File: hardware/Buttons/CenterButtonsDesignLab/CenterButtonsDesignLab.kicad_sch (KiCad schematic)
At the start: 6 parts, among them J1 Conn_01x01, J2 Conn_01x01, J3 Conn_01x03, SW1 SW_Push, SW2 SW_Push, SW3 SW_Push

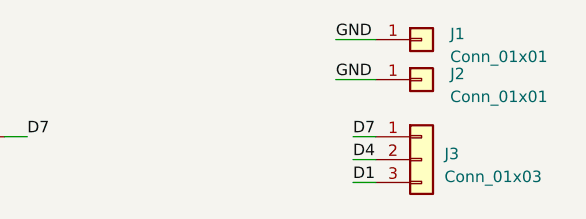
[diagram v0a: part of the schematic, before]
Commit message: BOM of buttons generated
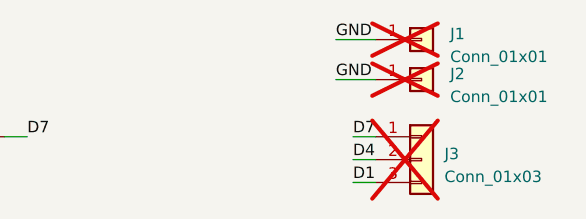
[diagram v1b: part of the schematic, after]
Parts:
- J1, J2, J3: now not fitted
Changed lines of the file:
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@@
   )
   (symbol (lib_id "Connector_Generic:Conn_01x01") (at 165.1 32.385 0) (unit 1)
-    (in_bom yes) (on_board yes) (dnp no) (fields_autoplaced)
+    (in_bom yes) (on_board yes) (dnp yes) (fields_autoplaced)
     (property "Reference" "J2" (at 168.275 31.75 0)
       (effects (font (size 1.27 1.27)) (justify left))
@@
   )
   (symbol (lib_id "Connector_Generic:Conn_01x03") (at 165.1 41.275 0) (unit 1)
-    (in_bom yes) (on_board yes) (dnp no) (fields_autoplaced)
+    (in_bom yes) (on_board yes) (dnp yes) (fields_autoplaced)
     (property "Reference" "J3" (at 167.64 40.64 0)
       (effects (font (size 1.27 1.27)) (justify left))
@@
   )
   (symbol (lib_id "Connector_Generic:Conn_01x01") (at 165.1 27.94 0) (unit 1)
-    (in_bom yes) (on_board yes) (dnp no) (fields_autoplaced)
+    (in_bom yes) (on_board yes) (dnp yes) (fields_autoplaced)
     (property "Reference" "J1" (at 168.275 27.305 0)
       (effects (font (size 1.27 1.27)) (justify left))

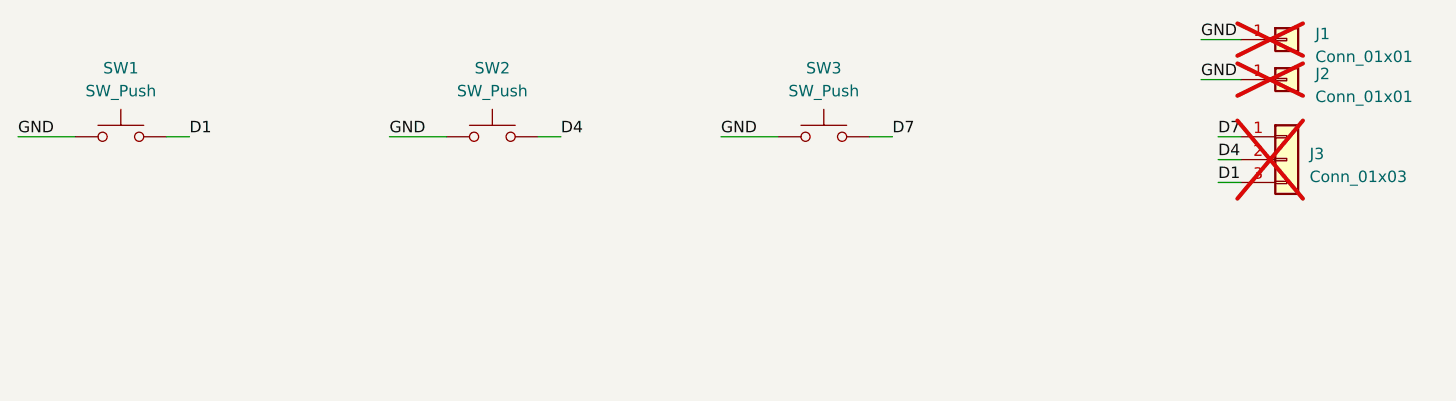
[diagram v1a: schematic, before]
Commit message: Changes of button started
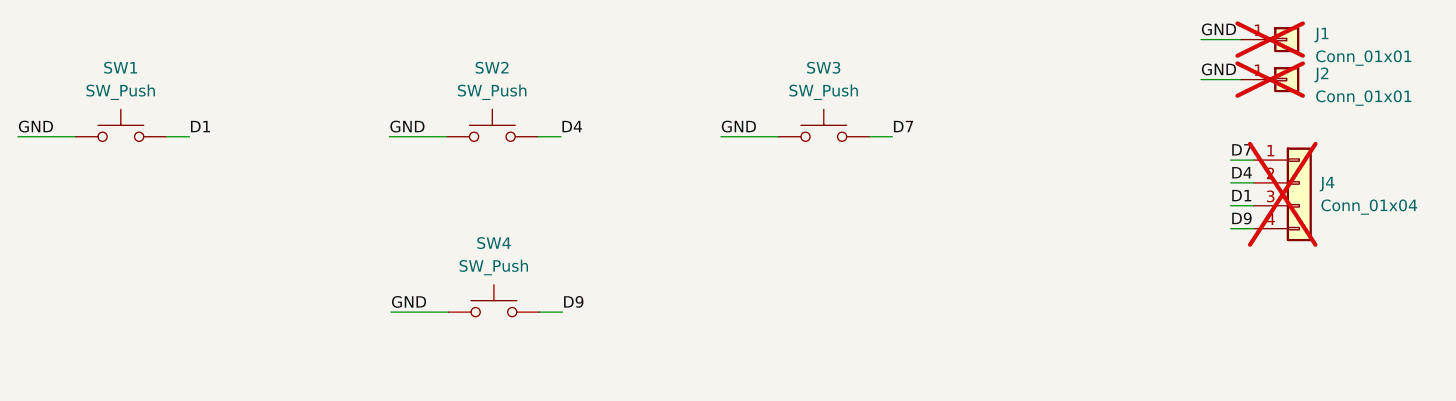
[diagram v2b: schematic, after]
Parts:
- removed J3: Conn_01x03, Connector_PinHeader_2.54mm:PinHeader_1x03_P2.54mm_Vertical, symbol Connector_Generic:Conn_01x03
- added J4: Conn_01x04, Connector_PinHeader_2.54mm:PinHeader_1x04_P2.54mm_Vertical, symbol Connector_Generic:Conn_01x04
- added SW4: SW_Push, Design:Button, symbol Switch:SW_Push
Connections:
- net D1: now also J4.3 (Pin_3)
- net D4: now also J4.2 (Pin_2)
- net D7: now also J4.1 (Pin_1)
- net GND: now also SW4.1
- new net D9: J4.4 (Pin_4), SW4.2
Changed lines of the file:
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@@
 (kicad_sch (version 20230121) (generator eeschema)
   (paper "A4")
+  (wire (pts (xy 65.5828 58.2168) (xy 71.9328 58.2168))
+    (stroke (width 0) (type default))
+  )
+  (wire (pts (xy 84.6328 58.2168) (xy 82.0928 58.2168))
+    (stroke (width 0) (type default))
+  )
   (wire (pts (xy 121.285 38.735) (xy 118.745 38.735))
     (stroke (width 0) (type default))
@@
     (stroke (width 0) (type default))
   )
-  (wire (pts (xy 157.48 38.735) (xy 160.02 38.735))
+  (wire (pts (xy 158.877 41.3258) (xy 161.417 41.3258))
     (stroke (width 0) (type default))
   )
@@
     (stroke (width 0) (type default))
   )
-  (wire (pts (xy 157.48 41.275) (xy 160.02 41.275))
-    (stroke (width 0) (type default))
-  )
-  (wire (pts (xy 157.48 43.815) (xy 160.02 43.815))
+  (wire (pts (xy 158.877 43.8658) (xy 161.417 43.8658))
+    (stroke (width 0) (type default))
+  )
+  (wire (pts (xy 158.877 46.4058) (xy 161.417 46.4058))
+    (stroke (width 0) (type default))
+  )
+  (wire (pts (xy 158.877 48.9458) (xy 161.417 48.9458))
     (stroke (width 0) (type default))
   )
@@
     (stroke (width 0) (type default))
   )
-  (label "D1" (at 157.48 43.815 0) (fields_autoplaced)
-    (effects (font (size 1.27 1.27)) (justify left bottom))
-  )
-  (label "D4" (at 157.48 41.275 0) (fields_autoplaced)
+  (label "D9" (at 84.6328 58.2168 0) (fields_autoplaced)
+    (effects (font (size 1.27 1.27)) (justify left bottom))
+  )
+  (label "D1" (at 158.877 46.4058 0) (fields_autoplaced)
+    (effects (font (size 1.27 1.27)) (justify left bottom))
+  )
+  (label "D4" (at 158.877 43.8658 0) (fields_autoplaced)
     (effects (font (size 1.27 1.27)) (justify left bottom))
   )
@@
     (effects (font (size 1.27 1.27)) (justify left bottom))
   )
-  (label "D7" (at 157.48 38.735 0) (fields_autoplaced)
+  (label "D7" (at 158.877 41.3258 0) (fields_autoplaced)
     (effects (font (size 1.27 1.27)) (justify left bottom))
   )
@@
     (effects (font (size 1.27 1.27)) (justify left bottom))
   )
+  (label "GND" (at 65.5828 58.2168 0) (fields_autoplaced)
+    (effects (font (size 1.27 1.27)) (justify left bottom))
+  )
   (label "GND" (at 24.13 38.735 0) (fields_autoplaced)
     (effects (font (size 1.27 1.27)) (justify left bottom))
@@
   )
   (label "GND" (at 102.235 38.735 0) (fields_autoplaced)
+    (effects (font (size 1.27 1.27)) (justify left bottom))
+  )
+  (label "D9" (at 158.877 48.9458 0) (fields_autoplaced)
     (effects (font (size 1.27 1.27)) (justify left bottom))
   )
@@
     )
   )
-  (symbol (lib_id "Connector_Generic:Conn_01x03") (at 165.1 41.275 0) (unit 1)
+  (symbol (lib_id "Connector_Generic:Conn_01x04") (at 166.497 43.8658 0) (unit 1)
     (in_bom yes) (on_board yes) (dnp yes) (fields_autoplaced)
-    (property "Reference" "J3" (at 167.64 40.64 0)
-      (effects (font (size 1.27 1.27)) (justify left))
-    )
-    (property "Value" "Conn_01x03" (at 167.64 43.18 0)
-      (effects (font (size 1.27 1.27)) (justify left))
-    )
-    (property "Footprint" "Connector_PinHeader_2.54mm:PinHeader_1x03_P2.54mm_Vertical" (at 165.1 41.275 0)
-      (effects (font (size 1.27 1.27)) hide)
-    )
-    (property "Datasheet" "~" (at 165.1 41.275 0)
+    (property "Reference" "J4" (at 168.8592 43.8658 0)
+      (effects (font (size 1.27 1.27)) (justify left))
+    )
+    (property "Value" "Conn_01x04" (at 168.8592 46.4058 0)
+      (effects (font (size 1.27 1.27)) (justify left))
+    )
+    (property "Footprint" "Connector_PinHeader_2.54mm:PinHeader_1x04_P2.54mm_Vertical" (at 166.497 43.8658 0)
+      (effects (font (size 1.27 1.27)) hide)
+    )
+    (property "Datasheet" "~" (at 166.497 43.8658 0)
       (effects (font (size 1.27 1.27)) hide)
     )
@@
     (pin "2")
     (pin "3")
-    (instances
-      (project "CenterButtonsDesignLab"
-        (path "/60a80ef2-fa88-492e-9ae7-a70a1d03dbe3"
-          (reference "J3") (unit 1)
-        )
-      )
-      (project "ButtonDesignLab"
-        (path "/e63e39d7-6ac0-4ffd-8aa3-1841a4541b55"
-          (reference "J3") (unit 1)
+    (pin "4")
+    (instances
+      (project "CenterButtonsDesignLab"
+        (path "/60a80ef2-fa88-492e-9ae7-a70a1d03dbe3"
+          (reference "J4") (unit 1)
         )
       )
@@
         )
       )
+    )
+  )
+  (symbol (lib_id "Switch:SW_Push") (at 77.0128 58.2168 0) (unit 1)
+    (in_bom yes) (on_board yes) (dnp no) (fields_autoplaced)
+    (property "Reference" "SW4" (at 77.0128 50.5968 0)
+      (effects (font (size 1.27 1.27)))
+    )
+    (property "Value" "SW_Push" (at 77.0128 53.1368 0)
+      (effects (font (size 1.27 1.27)))
+    )
+    (property "Footprint" "Design:Button" (at 77.0128 53.1368 0)
+      (effects (font (size 1.27 1.27)) hide)
+    )
+    (property "Datasheet" "https://datasheet.lcsc.com/lcsc/2210210930_BIWIN-TR12S_C5141768.pdf" (at 77.0128 53.1368 0)
+      (effects (font (size 1.27 1.27)) hide)
+    )
+    (property "LCSC#" "C5141768" (at 77.0128 58.2168 0)
+      (effects (font (size 1.27 1.27)) hide)
+    )
+    (property "Proveedor" "LCSC" (at 77.0128 58.2168 0)
+      (effects (font (size 1.27 1.27)) hide)
+    )
+    (pin "1")
+    (pin "2")
+    (instances
+      (project "CenterButtonsDesignLab"
+        (path "/60a80ef2-fa88-492e-9ae7-a70a1d03dbe3"
+          (reference "SW4") (unit 1)
+        )
+      )
+      (project "ButtonDesignLab"
+        (path "/e63e39d7-6ac0-4ffd-8aa3-1841a4541b55"
+          (reference "SW8") (unit 1)
+        )
+      )

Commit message: Update all PCB and schematics
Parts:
- removed J1, J2: Conn_01x01, Connector_PinHeader_2.54mm:PinHeader_1x01_P2.54mm_Vertical, symbol Connector_Generic:Conn_01x01
- removed J4: Conn_01x04, Connector_PinHeader_2.54mm:PinHeader_1x04_P2.54mm_Vertical, symbol Connector_Generic:Conn_01x04
- added J1: Conn_01x05, Design:JST_S5B-PH-K-S_LF__SN_, symbol Connector_Generic:Conn_01x05
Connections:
- net D1: now also J1.4 (Pin_4)
- net D4: now also J1.3 (Pin_3)
- net D7: now also J1.2 (Pin_2)
- net D9: now also J1.5 (Pin_5)
- net GND: now also J1.1 (Pin_1)
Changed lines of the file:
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@@
     (stroke (width 0) (type default))
   )
-  (wire (pts (xy 155.575 32.385) (xy 160.02 32.385))
+  (wire (pts (xy 156.845 48.895) (xy 160.655 48.895))
     (stroke (width 0) (type default))
   )
-  (wire (pts (xy 158.877 41.3258) (xy 161.417 41.3258))
-    (stroke (width 0) (type default))
-  )
-  (wire (pts (xy 155.575 27.94) (xy 160.02 27.94))
-    (stroke (width 0) (type default))
-  )
-  (wire (pts (xy 158.877 43.8658) (xy 161.417 43.8658))
-    (stroke (width 0) (type default))
-  )
-  (wire (pts (xy 158.877 46.4058) (xy 161.417 46.4058))
-    (stroke (width 0) (type default))
-  )
-  (wire (pts (xy 158.877 48.9458) (xy 161.417 48.9458))
+  (wire (pts (xy 156.845 56.515) (xy 160.655 56.515))
     (stroke (width 0) (type default))
   )
   (wire (pts (xy 102.235 38.735) (xy 108.585 38.735))
+    (stroke (width 0) (type default))
+  )
+  (wire (pts (xy 156.845 51.435) (xy 160.655 51.435))
+    (stroke (width 0) (type default))
+  )
+  (wire (pts (xy 156.845 59.055) (xy 160.655 59.055))
     (stroke (width 0) (type default))
   )
@@
     (stroke (width 0) (type default))
   )
+  (wire (pts (xy 156.845 53.975) (xy 160.655 53.975))
+    (stroke (width 0) (type default))
+  )
   (label "D9" (at 84.6328 58.2168 0) (fields_autoplaced)
     (effects (font (size 1.27 1.27)) (justify left bottom))
   )
-  (label "D1" (at 158.877 46.4058 0) (fields_autoplaced)
+  (label "GND" (at 156.845 48.895 0) (fields_autoplaced)
     (effects (font (size 1.27 1.27)) (justify left bottom))
   )
-  (label "D4" (at 158.877 43.8658 0) (fields_autoplaced)
+  (label "D1" (at 156.845 56.515 0) (fields_autoplaced)
+    (effects (font (size 1.27 1.27)) (justify left bottom))
+  )
+  (label "D4" (at 156.845 53.975 0) (fields_autoplaced)
     (effects (font (size 1.27 1.27)) (justify left bottom))
   )
@@
     (effects (font (size 1.27 1.27)) (justify left bottom))
   )
-  (label "GND" (at 155.575 32.385 0) (fields_autoplaced)
-    (effects (font (size 1.27 1.27)) (justify left bottom))
-  )
-  (label "D7" (at 158.877 41.3258 0) (fields_autoplaced)
+  (label "D7" (at 156.845 51.435 0) (fields_autoplaced)
     (effects (font (size 1.27 1.27)) (justify left bottom))
   )
@@
     (effects (font (size 1.27 1.27)) (justify left bottom))
   )
-  (label "D9" (at 158.877 48.9458 0) (fields_autoplaced)
+  (label "D9" (at 156.845 59.055 0) (fields_autoplaced)
     (effects (font (size 1.27 1.27)) (justify left bottom))
   )
@@
     (effects (font (size 1.27 1.27)) (justify left bottom))
   )
-  (label "GND" (at 155.575 27.94 0) (fields_autoplaced)
-    (effects (font (size 1.27 1.27)) (justify left bottom))
+  (symbol (lib_id "Connector_Generic:Conn_01x05") (at 165.735 53.975 0) (unit 1)
+    (in_bom yes) (on_board yes) (dnp no)
+    (property "Reference" "J1" (at 165.735 64.77 0)
+      (effects (font (size 1.27 1.27)))
+    )
+    (property "Value" "Conn_01x05" (at 165.735 62.23 0)
+      (effects (font (size 1.27 1.27)))
+    )
+    (property "Footprint" "Design:JST_S5B-PH-K-S_LF__SN_" (at 165.735 53.975 0)
+      (effects (font (size 1.27 1.27)) hide)
+    )
+    (property "Datasheet" "https://datasheet.lcsc.com/lcsc/2304140030_JST-S5B-PH-K-S-LF-SN_C157923.pdf" (at 165.735 53.975 0)
+      (effects (font (size 1.27 1.27)) hide)
+    )
+    (property "LCSC#" "C157923" (at 165.735 53.975 0)
+      (effects (font (size 1.27 1.27)) hide)
+    )
+    (pin "1")
+    (pin "2")
+    (pin "3")
+    (pin "4")
+    (pin "5")
+    (instances
+      (project "CenterButtonsDesignLab"
+        (path "/60a80ef2-fa88-492e-9ae7-a70a1d03dbe3"
+          (reference "J1") (unit 1)
+        )
+      )
+    )
   )
   (symbol (lib_id "Switch:SW_Push") (at 76.835 38.735 0) (unit 1)
@@
         )
       )
-    )
-  )
-  (symbol (lib_id "Connector_Generic:Conn_01x01") (at 165.1 32.385 0) (unit 1)
-    (in_bom yes) (on_board yes) (dnp yes) (fields_autoplaced)
-    (property "Reference" "J2" (at 168.275 31.75 0)
-      (effects (font (size 1.27 1.27)) (justify left))
-    )
-    (property "Value" "Conn_01x01" (at 168.275 34.29 0)
-      (effects (font (size 1.27 1.27)) (justify left))
-    )
-    (property "Footprint" "Connector_PinHeader_2.54mm:PinHeader_1x01_P2.54mm_Vertical" (at 165.1 32.385 0)
-      (effects (font (size 1.27 1.27)) hide)
-    )
-    (property "Datasheet" "~" (at 165.1 32.385 0)
-      (effects (font (size 1.27 1.27)) hide)
-    )
-    (pin "1")
-    (instances
-      (project "CenterButtonsDesignLab"
-        (path "/60a80ef2-fa88-492e-9ae7-a70a1d03dbe3"
-          (reference "J2") (unit 1)
-        )
-      )
-      (project "ButtonDesignLab"
-        (path "/e63e39d7-6ac0-4ffd-8aa3-1841a4541b55"
-          (reference "J4") (unit 1)
-        )
-      )
-    )
-  )
-  (symbol (lib_id "Connector_Generic:Conn_01x04") (at 166.497 43.8658 0) (unit 1)
-    (in_bom yes) (on_board yes) (dnp yes) (fields_autoplaced)
-    (property "Reference" "J4" (at 168.8592 43.8658 0)
-      (effects (font (size 1.27 1.27)) (justify left))
-    )
-    (property "Value" "Conn_01x04" (at 168.8592 46.4058 0)
-      (effects (font (size 1.27 1.27)) (justify left))
-    )
-    (property "Footprint" "Connector_PinHeader_2.54mm:PinHeader_1x04_P2.54mm_Vertical" (at 166.497 43.8658 0)
-      (effects (font (size 1.27 1.27)) hide)
-    )
-    (property "Datasheet" "~" (at 166.497 43.8658 0)
-      (effects (font (size 1.27 1.27)) hide)
-    )
-    (pin "1")
-    (pin "2")
-    (pin "3")
-    (pin "4")
-    (instances
-      (project "CenterButtonsDesignLab"
-        (path "/60a80ef2-fa88-492e-9ae7-a70a1d03dbe3"
-          (reference "J4") (unit 1)
-        )
-      )
-    )
-  )
-  (symbol (lib_id "Connector_Generic:Conn_01x01") (at 165.1 27.94 0) (unit 1)
-    (in_bom yes) (on_board yes) (dnp yes) (fields_autoplaced)
-    (property "Reference" "J1" (at 168.275 27.305 0)
-      (effects (font (size 1.27 1.27)) (justify left))
-    )
-    (property "Value" "Conn_01x01" (at 168.275 29.845 0)
-      (effects (font (size 1.27 1.27)) (justify left))
-    )
-    (property "Footprint" "Connector_PinHeader_2.54mm:PinHeader_1x01_P2.54mm_Vertical" (at 165.1 27.94 0)
-      (effects (font (size 1.27 1.27)) hide)
-    )
-    (property "Datasheet" "~" (at 165.1 27.94 0)
-      (effects (font (size 1.27 1.27)) hide)
-    )
-    (pin "1")
-    (instances
-      (project "CenterButtonsDesignLab"
-        (path "/60a80ef2-fa88-492e-9ae7-a70a1d03dbe3"
-          (reference "J1") (unit 1)
-        )
-      )
-      (project "ButtonDesignLab"
-        (path "/e63e39d7-6ac0-4ffd-8aa3-1841a4541b55"
-          (reference "J5") (unit 1)
-        )
-      )

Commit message: Update PCB
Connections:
- net D1: now also J1.3 (Pin_3); no longer J1.4 (Pin_4)
- net D4: now also J1.4 (Pin_4); no longer J1.3 (Pin_3)
- net D7: now also J1.5 (Pin_5); no longer J1.2 (Pin_2)
- net D9: now also J1.2 (Pin_2); no longer J1.5 (Pin_5)
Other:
- moved on the sheet: J1
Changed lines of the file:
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@@
     (stroke (width 0) (type default))
   )
-  (wire (pts (xy 156.845 48.895) (xy 160.655 48.895))
+  (wire (pts (xy 158.75 59.055) (xy 162.56 59.055))
     (stroke (width 0) (type default))
   )
-  (wire (pts (xy 156.845 56.515) (xy 160.655 56.515))
+  (wire (pts (xy 158.75 53.975) (xy 162.56 53.975))
     (stroke (width 0) (type default))
   )
@@
     (stroke (width 0) (type default))
   )
-  (wire (pts (xy 156.845 51.435) (xy 160.655 51.435))
+  (wire (pts (xy 158.75 48.895) (xy 162.56 48.895))
     (stroke (width 0) (type default))
   )
-  (wire (pts (xy 156.845 59.055) (xy 160.655 59.055))
+  (wire (pts (xy 158.75 56.515) (xy 162.56 56.515))
     (stroke (width 0) (type default))
   )
@@
     (stroke (width 0) (type default))
   )
-  (wire (pts (xy 156.845 53.975) (xy 160.655 53.975))
+  (wire (pts (xy 158.75 51.435) (xy 162.56 51.435))
     (stroke (width 0) (type default))
   )
@@
     (effects (font (size 1.27 1.27)) (justify left bottom))
   )
-  (label "GND" (at 156.845 48.895 0) (fields_autoplaced)
+  (label "GND" (at 158.75 59.055 0) (fields_autoplaced)
     (effects (font (size 1.27 1.27)) (justify left bottom))
   )
-  (label "D1" (at 156.845 56.515 0) (fields_autoplaced)
+  (label "D1" (at 158.75 53.975 0) (fields_autoplaced)
     (effects (font (size 1.27 1.27)) (justify left bottom))
   )
-  (label "D4" (at 156.845 53.975 0) (fields_autoplaced)
+  (label "D4" (at 158.75 51.435 0) (fields_autoplaced)
     (effects (font (size 1.27 1.27)) (justify left bottom))
   )
@@
     (effects (font (size 1.27 1.27)) (justify left bottom))
   )
-  (label "D7" (at 156.845 51.435 0) (fields_autoplaced)
+  (label "D7" (at 158.75 48.895 0) (fields_autoplaced)
     (effects (font (size 1.27 1.27)) (justify left bottom))
   )
@@
     (effects (font (size 1.27 1.27)) (justify left bottom))
   )
-  (label "D9" (at 156.845 59.055 0) (fields_autoplaced)
+  (label "D9" (at 158.75 56.515 0) (fields_autoplaced)
     (effects (font (size 1.27 1.27)) (justify left bottom))
   )
@@
     (effects (font (size 1.27 1.27)) (justify left bottom))
   )
-  (symbol (lib_id "Connector_Generic:Conn_01x05") (at 165.735 53.975 0) (unit 1)
+  (symbol (lib_id "Connector_Generic:Conn_01x05") (at 167.64 53.975 0) (mirror x) (unit 1)
     (in_bom yes) (on_board yes) (dnp no)
-    (property "Reference" "J1" (at 165.735 64.77 0)
+    (property "Reference" "J1" (at 167.64 43.18 0)
       (effects (font (size 1.27 1.27)))
     )
-    (property "Value" "Conn_01x05" (at 165.735 62.23 0)
+    (property "Value" "Conn_01x05" (at 167.64 45.72 0)
       (effects (font (size 1.27 1.27)))
     )
-    (property "Footprint" "Design:JST_S5B-PH-K-S_LF__SN_" (at 165.735 53.975 0)
+    (property "Footprint" "Design:JST_S5B-PH-K-S_LF__SN_" (at 167.64 53.975 0)
       (effects (font (size 1.27 1.27)) hide)
     )
-    (property "Datasheet" "https://datasheet.lcsc.com/lcsc/2304140030_JST-S5B-PH-K-S-LF-SN_C157923.pdf" (at 165.735 53.975 0)
+    (property "Datasheet" "https://datasheet.lcsc.com/lcsc/2304140030_JST-S5B-PH-K-S-LF-SN_C157923.pdf" (at 167.64 53.975 0)
       (effects (font (size 1.27 1.27)) hide)
     )
-    (property "LCSC#" "C157923" (at 165.735 53.975 0)
+    (property "LCSC#" "C157923" (at 167.64 53.975 0)
       (effects (font (size 1.27 1.27)) hide)
     )
